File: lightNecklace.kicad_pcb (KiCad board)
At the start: 2 copper layers, 0 parts

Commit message: Added button footprint
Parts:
- added G***: LOGO, BashPCB:trebleCleffScaled, F.Cu at (142.5, 111.5)

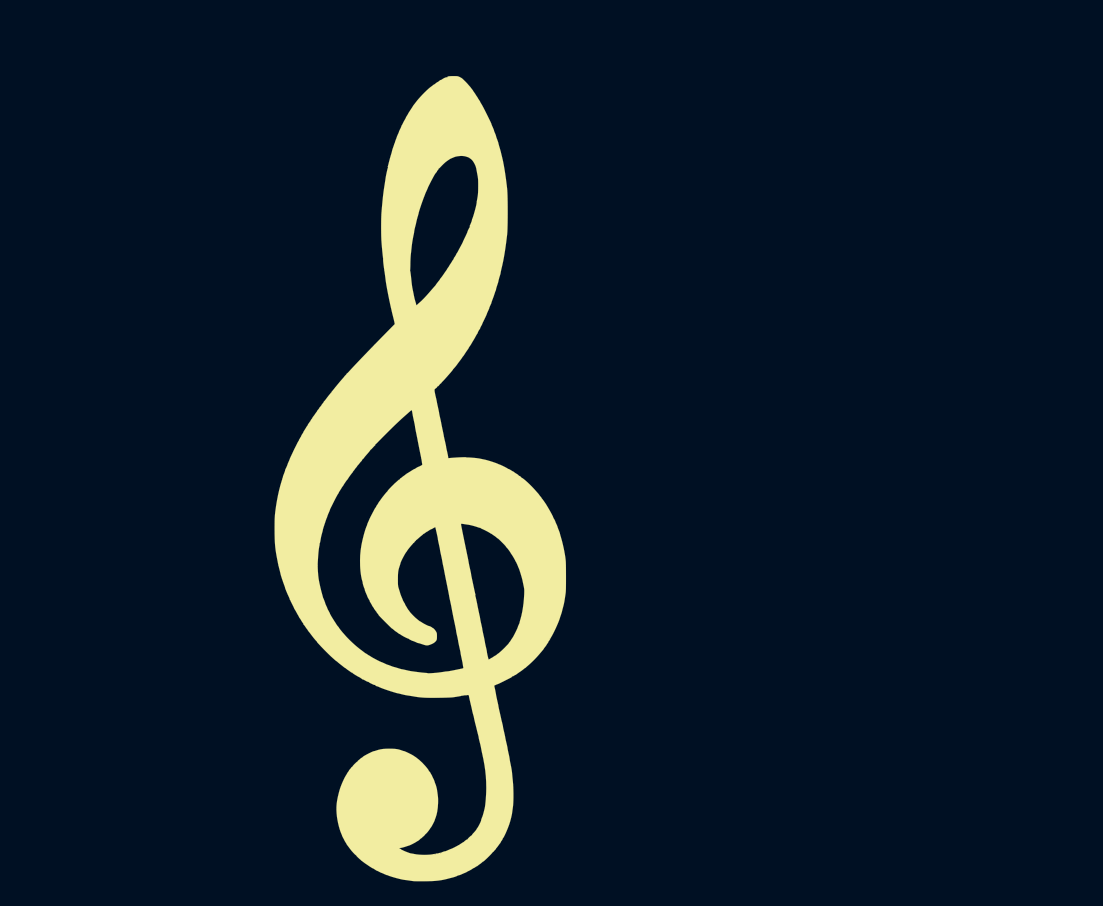
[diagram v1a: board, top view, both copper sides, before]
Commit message: Finished CVPCB
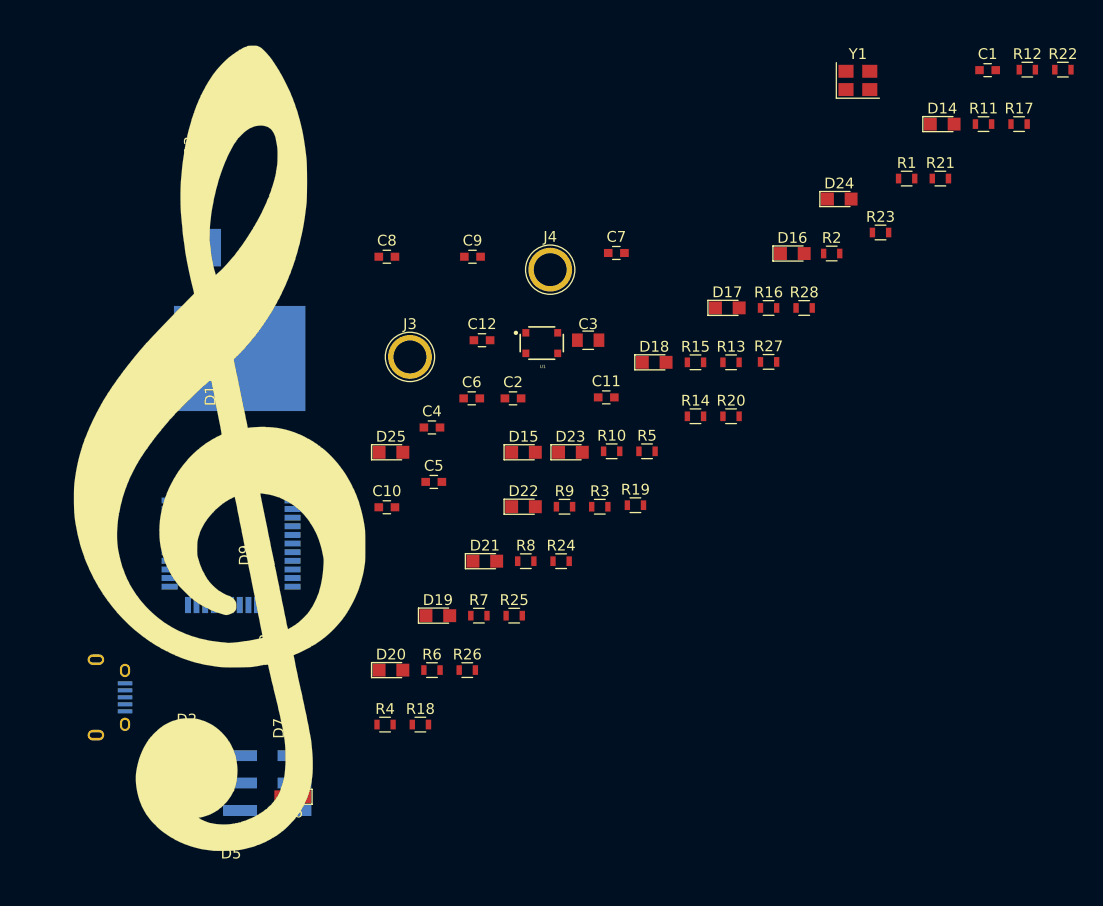
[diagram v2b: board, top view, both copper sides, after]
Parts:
- added C1: 12pF, Capacitors_SMD:C_0603, F.Cu at (195.1, 73.6)
- added C10: .1uF, Capacitors_SMD:C_0603, F.Cu at (139.4, 114.1)
- added C11: .33uF, Capacitors_SMD:C_0603, F.Cu at (159.7, 103.9)
- added C12: 0.33uF, Capacitors_SMD:C_0603, F.Cu at (148.2, 98.6)
- added C2: 12pF, Capacitors_SMD:C_0603, F.Cu at (151.1, 104.0)
- added C3: 10uF, Capacitors_SMD:C_0805, F.Cu at (158.0, 98.6)
- added C4: 1uF, Capacitors_SMD:C_0603, F.Cu at (143.6, 106.7)
- added C5: .1uF, Capacitors_SMD:C_0603, F.Cu at (143.7, 111.8)
- added C6: .1uF, Capacitors_SMD:C_0603, F.Cu at (147.2, 104.0)
- added C7: .1uF, Capacitors_SMD:C_0603, F.Cu at (160.7, 90.5)
- added C8: .1uF, Capacitors_SMD:C_0603, F.Cu at (139.4, 90.9)
- added C9: .1uF, Capacitors_SMD:C_0603, F.Cu at (147.3, 90.9)
- added D1: LED, LEDs:LED_0805, F.Cu at (124.5, 138.6)
- added D10: LED, LEDs:LED_0805, F.Cu at (126.4, 110.3)
- added D11: LED, LEDs:LED_0805, F.Cu at (124.5, 103.3)
- added D12: LED, LEDs:LED_0805, F.Cu at (123.2, 96.3)
- added D13: LED, LEDs:LED_0805, F.Cu at (122.6, 81.1)
- added D14: LED, LEDs:LED_0805, F.Cu at (190.9, 78.6)
- added D15: LED, LEDs:LED_0805, F.Cu at (152.0, 109.0)
- added D16: LED, LEDs:LED_0805, F.Cu at (177.0, 90.6)
- added D17: LED, LEDs:LED_0805, F.Cu at (170.9, 95.6)
- added D18: LED, LEDs:LED_0805, F.Cu at (164.2, 100.7)
- added D19: LED, LEDs:LED_0805, F.Cu at (144.1, 124.2)
- added D2: LED, LEDs:LED_0805, F.Cu at (120.8, 135.3)
- added D20: LED, LEDs:LED_0805, F.Cu at (139.8, 129.2)
- added D21: LED, LEDs:LED_0805, F.Cu at (148.5, 119.1)
- added D22: LED, LEDs:LED_0805, F.Cu at (152.0, 114.1)
- added D23: LED, LEDs:LED_0805, F.Cu at (156.4, 109.0)
- added D24: LED, LEDs:LED_0805, F.Cu at (181.3, 85.5)
- added D25: LED, LEDs:LED_0805, F.Cu at (139.8, 109.0)
- added D3: LED, LEDs:LED_0805, F.Cu at (117.5, 138.6)
- added D4: LED, LEDs:LED_0805, F.Cu at (121.1, 141.6)
- added D5: LED, LEDs:LED_0805, F.Cu at (124.9, 144.8)
- added D6: LED, LEDs:LED_0805, F.Cu at (130.6, 141.0)
- added D7: LED, LEDs:LED_0805, F.Cu at (130.8, 134.6)
- added D8: LED, LEDs:LED_0805, F.Cu at (129.5, 126.8)
- added D9: LED, LEDs:LED_0805, F.Cu at (127.6, 118.6)
- added J1: USB_OTG, Connectors:USB_Micro-B, B.Cu at (113.7, 131.8)
- added J2: CONN_02X03, Pin_Headers:Pin_Header_Straight_2x03_Pitch2.54mm_SMD, B.Cu at (128.3, 139.7)
- added J3: PowerBatt, Connectors:1pin, F.Cu at (141.5, 100.2)
- added J4: GroundBatt, Connectors:1pin, F.Cu at (154.5, 92.1)
- added R1: 22, Resistors_SMD:R_0603, F.Cu at (187.6, 83.6)
- added R10: 400, Resistors_SMD:R_0603, F.Cu at (160.2, 108.9)
- added R11: 400, Resistors_SMD:R_0603, F.Cu at (194.7, 78.6)
- added R12: 400, Resistors_SMD:R_0603, F.Cu at (198.8, 73.5)
- added R13: 400, Resistors_SMD:R_0603, F.Cu at (171.3, 100.7)
- added R14: 400, Resistors_SMD:R_0603, F.Cu at (168.0, 105.7)
- added R15: 400, Resistors_SMD:R_0603, F.Cu at (168.0, 100.7)
- added R16: 400, Resistors_SMD:R_0603, F.Cu at (174.8, 95.6)
- added R17: 400, Resistors_SMD:R_0603, F.Cu at (198.0, 78.6)
- added R18: 400, Resistors_SMD:R_0603, F.Cu at (142.5, 134.3)
- added R19: 400, Resistors_SMD:R_0603, F.Cu at (162.4, 113.9)
- added R2: 22, Resistors_SMD:R_0603, F.Cu at (180.6, 90.6)
- added R20: 400, Resistors_SMD:R_0603, F.Cu at (171.3, 105.7)
- added R21: 400, Resistors_SMD:R_0603, F.Cu at (190.7, 83.6)
- added R22: 400, Resistors_SMD:R_0603, F.Cu at (202.1, 73.5)
- added R23: 400, Resistors_SMD:R_0603, F.Cu at (185.2, 88.6)
- added R24: 400, Resistors_SMD:R_0603, F.Cu at (155.5, 119.1)
- added R25: 400, Resistors_SMD:R_0603, F.Cu at (151.2, 124.2)
- added R26: 400, Resistors_SMD:R_0603, F.Cu at (146.8, 129.2)
- added R27: 400, Resistors_SMD:R_0603, F.Cu at (174.8, 100.6)
- added R28: 400, Resistors_SMD:R_0603, F.Cu at (178.1, 95.6)
- added R3: 10K, Resistors_SMD:R_0603, F.Cu at (159.1, 114.1)
- added R4: 400, Resistors_SMD:R_0603, F.Cu at (139.2, 134.3)
- added R5: 400, Resistors_SMD:R_0603, F.Cu at (163.5, 108.9)
- added R6: 400, Resistors_SMD:R_0603, F.Cu at (143.6, 129.2)
- added R7: 400, Resistors_SMD:R_0603, F.Cu at (147.9, 124.2)
- added R8: 400, Resistors_SMD:R_0603, F.Cu at (152.3, 119.1)
- added R9: 400, Resistors_SMD:R_0603, F.Cu at (155.8, 114.1)
- added U1: button, BashPCB:KMT071_NGJ_LHS, F.Cu at (153.7, 98.9)
- added U2: ATMEGA32U4RC-AU, Housings_QFP:TQFP-44_10x10mm_Pitch0.8mm, B.Cu at (124.9, 117.5)
- added U3: 7805, BashPCB:D2PAK, B.Cu at (125.7, 100.3)
- added Y1: Crystal_GND24, Crystals:Crystal_SMD_3225-4pin_3.2x2.5mm, F.Cu at (183.1, 74.5)
- moved G*** 18.8 mm to (123.9, 108.7)

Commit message: Made edge cuts
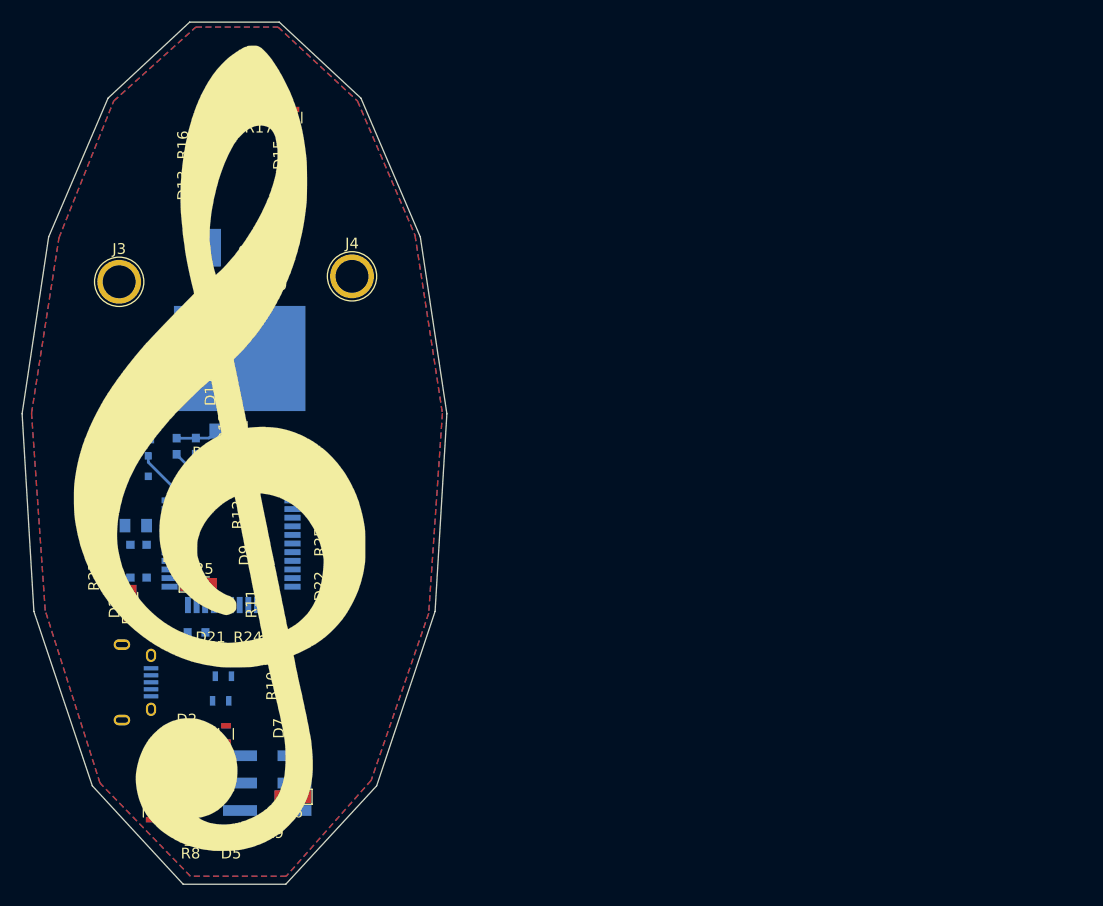
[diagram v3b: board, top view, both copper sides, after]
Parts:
- C1, C10, C11, C2, C3, C4, C5, C6, C7, C8, C9, R1, R2, R3, U1, Y1: moved to B.Cu
- C12: value 0.33uF -> 0.1uF
- moved R22 99.1 mm to (112.9, 116.8), turned to 180 degrees
- moved R12 82.8 mm to (127.0, 114.8), turned to 90 degrees
- moved R21 80.7 mm to (114.4, 109.9)
- moved R11 79.9 mm to (128.3, 123.1), turned to 90 degrees
- moved R1 78.4 mm to (124.2, 129.8), turned to 180 degrees
- moved R23 78.3 mm to (113.7, 120.5), turned to 90 degrees
- moved C1 76.5 mm to (127.0, 108.5), turned to 270 degrees
- moved R17 70.5 mm to (127.5, 77.5), turned to 180 degrees
- moved R2 70.2 mm to (124.0, 132.1), turned to 180 degrees
- moved Y1 67.6 mm to (124.4, 108.2), turned to 270 degrees
- moved D24 66.4 mm to (121.3, 113.8), turned to 90 degrees
- moved D14 63.8 mm to (127.2, 75.6)
- moved R28 61.6 mm to (120.7, 118.0), turned to 90 degrees
- moved R18 57.5 mm to (130.8, 78.0), turned to 90 degrees
- moved R16 55.0 mm to (121.9, 80.5), turned to 90 degrees
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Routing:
- net GND: track 0.00 -> 18.0 mm, vias 0 -> 7
- net Net-(C1-Pad1): track 0.00 -> 8.74 mm
- net /RESET: track 0.00 -> 7.21 mm
- net Net-(C2-Pad1): track 0.00 -> 4.66 mm
- net +5V: track 0.00 -> 4.31 mm
- net Net-(D8-Pad2): track 0.00 -> 2.56 mm
- net Net-(D22-Pad2): track 0.00 -> 2.25 mm
- added copper zone on F.Cu, net +5V
- added copper zone on B.Cu, net GND
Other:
- board outline added: 39.4 x 79.9 mm

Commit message: Finished Board
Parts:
- C12: moved to B.Cu
- moved J3 1.22 mm to (114.6, 92.0)
- moved J4 0.71 mm to (136.1, 92.0)
- moved C12 0.26 mm to (130.6, 89.4), turned to 270 degrees
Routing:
- net GND: track 18.0 -> 196.2 mm, vias 7 -> 43
- net /RESET: track 7.21 -> 74.2 mm
- net /LED3: track 0.00 -> 50.6 mm, vias 0 -> 1
- net /LED14: track 0.00 -> 44.8 mm, vias 0 -> 1
- net /MISO: track 0.00 -> 42.1 mm
- net +5V: track 4.31 -> 45.7 mm, vias 0 -> 13
- net /LED15: track 0.00 -> 40.0 mm, vias 0 -> 1
- net /LED2: track 0.00 -> 40.0 mm, vias 0 -> 2
- net /LED13: track 0.00 -> 39.0 mm, vias 0 -> 1
- net /LED5: track 0.00 -> 35.2 mm, vias 0 -> 1
- net Net-(R1-Pad1): track 0.00 -> 34.4 mm
- net /LED7: track 0.00 -> 34.2 mm, vias 0 -> 1
- net /LED4: track 0.00 -> 29.6 mm, vias 0 -> 1
- net /LED6: track 0.00 -> 27.5 mm, vias 0 -> 1
- net /LED16: track 0.00 -> 25.5 mm, vias 0 -> 1
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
